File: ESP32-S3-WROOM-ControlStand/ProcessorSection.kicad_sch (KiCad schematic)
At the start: 21 parts, among them IC601 USBLC6-2SC6, J601 GCT_USB4105, SW24 RESET, SW601 BOOT, U601 ESP32_S3_WROOM-1

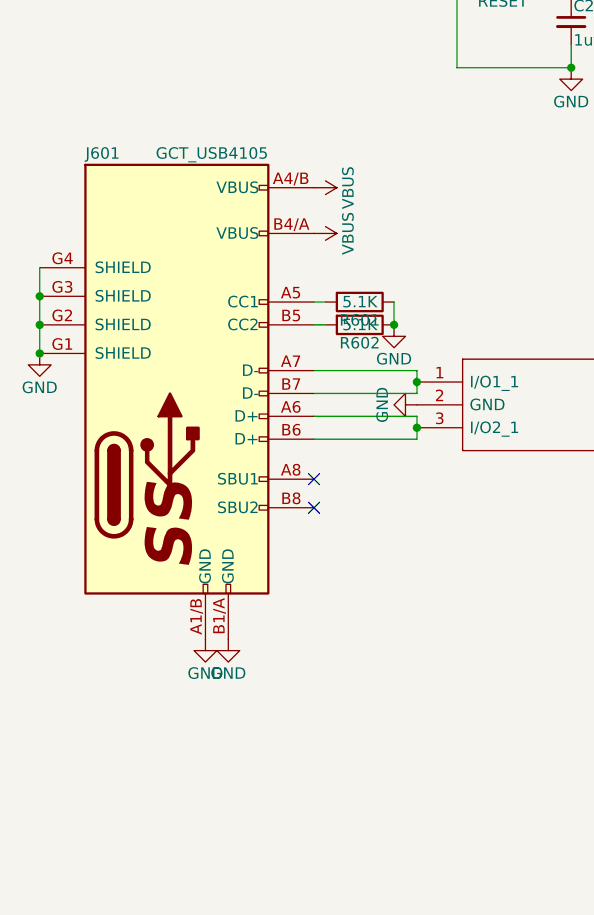
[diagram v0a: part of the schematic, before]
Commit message: 3D models mostly done.
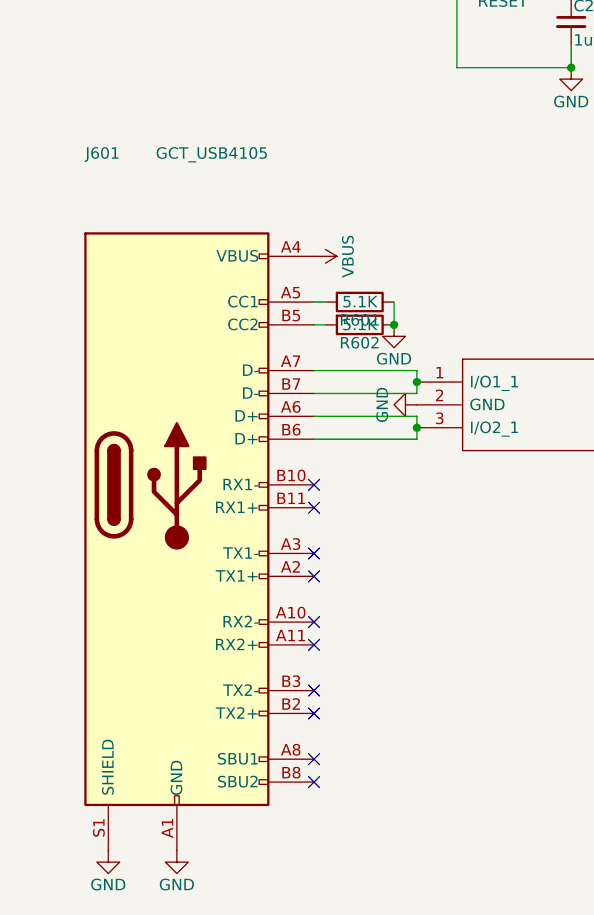
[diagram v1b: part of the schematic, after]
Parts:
- IC601: footprint TO_SOT_Packages_SMD:SOT-23-6 -> Package_TO_SOT_SMD:SOT-23-6
- J601: footprint GCT_USB:GCT_USB4105-GF-A -> Connector_USB:USB_C_Receptacle_GCT_USB4105-xx-A_16P_TopMnt_Horizontal; symbol gct_usb4105:GCT_USB4105 -> Connector:USB_C_Receptacle
- SW24: footprint Buttons_Switches_SMD:SW_SPST_PTS810 -> Button_Switch_SMD:SW_SPST_PTS810
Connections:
- net GND: now also J601.A1 (GND), J601.A12 (GND), J601.B1 (GND), J601.B12 (GND), J601.S1 (SHIELD); no longer J601.A1/B (GND), J601.B1/A (GND), J601.G1 (SHIELD), J601.G2 (SHIELD), J601.G3 (SHIELD), J601.G4 (SHIELD)
- net VBUS: now also J601.A4 (VBUS), J601.A9 (VBUS), J601.B4 (VBUS), J601.B9 (VBUS); no longer J601.A4/B (VBUS), J601.B4/A (VBUS)
- no-connect marks 12 -> 20
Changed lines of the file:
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@@
   (junction (at 73.025 139.065) (diameter 0) (color 0 0 0 0)
   )
-  (junction (at 33.655 135.89) (diameter 0) (color 0 0 0 0)
-  )
-  (junction (at 33.655 139.065) (diameter 0) (color 0 0 0 0)
-  )
   (junction (at 75.565 150.495) (diameter 0) (color 0 0 0 0)
   )
@@
   (junction (at 92.71 110.49) (diameter 0) (color 0 0 0 0)
   )
-  (junction (at 33.655 142.24) (diameter 0) (color 0 0 0 0)
-  )
   (junction (at 167.005 66.04) (diameter 0) (color 0 0 0 0)
   )
   (junction (at 92.71 101.6) (diameter 0) (color 0 0 0 0)
   )
+  (no_connect (at 64.135 174.625))
+  (no_connect (at 64.135 182.245))
   (no_connect (at 192.405 82.55))
+  (no_connect (at 64.135 187.325))
+  (no_connect (at 64.135 179.705))
   (no_connect (at 192.405 90.17))
   (no_connect (at 192.405 95.25))
   (no_connect (at 64.135 159.385))
+  (no_connect (at 64.135 167.005))
   (no_connect (at 192.405 92.71))
   (no_connect (at 192.405 102.87))
-  (no_connect (at 64.135 156.21))
+  (no_connect (at 64.135 164.465))
+  (no_connect (at 64.135 156.845))
   (no_connect (at 192.405 105.41))
+  (no_connect (at 64.135 189.865))
   (no_connect (at 141.605 87.63))
   (no_connect (at 192.405 100.33))
+  (no_connect (at 64.135 172.085))
   (no_connect (at 192.405 87.63))
   (no_connect (at 192.405 85.09))
@@
     (stroke (width 0) (type default) (color 0 0 0 0))
   )
-  (wire (pts (xy 33.655 132.715) (xy 33.655 135.89))
-    (stroke (width 0) (type default) (color 0 0 0 0))
-  )
   (wire (pts (xy 73.025 136.525) (xy 73.025 139.065))
     (stroke (width 0) (type default) (color 0 0 0 0))
   )
-  (wire (pts (xy 33.655 135.89) (xy 33.655 139.065))
-    (stroke (width 0) (type default) (color 0 0 0 0))
-  )
   (wire (pts (xy 92.71 107.95) (xy 92.71 110.49))
     (stroke (width 0) (type default) (color 0 0 0 0))
@@
   )
   (wire (pts (xy 205.74 107.95) (xy 205.74 110.49))
-    (stroke (width 0) (type default) (color 0 0 0 0))
-  )
-  (wire (pts (xy 33.655 139.065) (xy 33.655 142.24))
     (stroke (width 0) (type default) (color 0 0 0 0))
   )
@@
     )
     (property "Value" "RESET" (id 1) (at 85.09 103.124 0))
-    (property "Footprint" "Buttons_Switches_SMD:SW_SPST_PTS810" (id 2) (at 85.09 96.52 0)
+    (property "Footprint" "Button_Switch_SMD:SW_SPST_PTS810" (id 2) (at 85.09 96.52 0)
       (effects (font (size 1.27 1.27)) hide)
     )
@@
     (pin "EPad")
   )
-  (symbol (lib_id "gct_usb4105:GCT_USB4105") (at 48.895 156.845 0) (unit 1)
+  (symbol (lib_id "Connector:USB_C_Receptacle") (at 48.895 156.845 0) (unit 1)
     (in_bom yes) (on_board yes)
     (property "Reference" "J601" (id 0) (at 38.735 120.015 0)
@@
       (effects (font (size 1.27 1.27)) (justify right))
     )
-    (property "Footprint" "GCT_USB:GCT_USB4105-GF-A" (id 2) (at 52.705 156.845 0)
-      (effects (font (size 1.27 1.27)) hide)
-    )
-    (property "Datasheet" "" (id 3) (at 52.705 156.845 0)
-      (effects (font (size 1.27 1.27)) hide)
-    )
-    (pin "A1/B")
-    (pin "A4/B")
+    (property "Footprint" "Connector_USB:USB_C_Receptacle_GCT_USB4105-xx-A_16P_TopMnt_Horizontal" (id 2) (at 52.705 156.845 0)
+      (effects (font (size 1.27 1.27)) hide)
+    )
+    (property "Datasheet" "https://www.usb.org/sites/default/files/documents/usb_type-c.zip" (id 3) (at 52.705 156.845 0)
+      (effects (font (size 1.27 1.27)) hide)
+    )
+    (pin "A1")
+    (pin "A10")
+    (pin "A11")
+    (pin "A12")
+    (pin "A2")
+    (pin "A3")
+    (pin "A4")
     (pin "A5")
     (pin "A6")
     (pin "A7")
     (pin "A8")
-    (pin "B1/A")
-    (pin "B4/A")
+    (pin "A9")
+    (pin "B1")
+    (pin "B10")
+    (pin "B11")
+    (pin "B12")
+    (pin "B2")
+    (pin "B3")
+    (pin "B4")
     (pin "B5")
     (pin "B6")
     (pin "B7")
     (pin "B8")
-    (pin "G1")
-    (pin "G2")
-    (pin "G3")
-    (pin "G4")
+    (pin "B9")
+    (pin "S1")
   )
   (symbol (lib_id "USBLC6-2SC6:USBLC6-2SC6") (at 75.565 145.415 0) (unit 1)
@@
       (effects (font (size 1.27 1.27)) (justify left))
     )
-    (property "Footprint" "TO_SOT_Packages_SMD:SOT-23-6" (id 2) (at 104.775 142.875 0)
+    (property "Footprint" "Package_TO_SOT_SMD:SOT-23-6" (id 2) (at 104.775 142.875 0)
       (effects (font (size 1.27 1.27)) (justify left) hide)
     )
@@
     (pin "1")
   )
-  (symbol (lib_id "ESP32-S3-WROOM-ControlStand-rescue:VBUS") (at 64.135 123.825 270) (unit 1)
-    (in_bom yes) (on_board yes)
-    (property "Reference" "#PWR071" (id 0) (at 60.325 123.825 0)
-      (effects (font (size 1.27 1.27)) hide)
-    )
-    (property "Value" "VBUS" (id 1) (at 67.945 123.825 0))
-    (property "Footprint" "" (id 2) (at 64.135 123.825 0)
-      (effects (font (size 1.27 1.27)) hide)
-    )
-    (property "Datasheet" "" (id 3) (at 64.135 123.825 0)
-      (effects (font (size 1.27 1.27)) hide)
-    )
-    (pin "1")
-  )
-  (symbol (lib_id "ESP32-S3-WROOM-ControlStand-rescue:VBUS") (at 64.135 128.905 270) (unit 1)
-    (in_bom yes) (on_board yes)
-    (property "Reference" "#PWR072" (id 0) (at 60.325 128.905 0)
-      (effects (font (size 1.27 1.27)) hide)
-    )
-    (property "Value" "VBUS" (id 1) (at 67.945 128.905 0))
-    (property "Footprint" "" (id 2) (at 64.135 128.905 0)
-      (effects (font (size 1.27 1.27)) hide)
-    )
-    (property "Datasheet" "" (id 3) (at 64.135 128.905 0)
-      (effects (font (size 1.27 1.27)) hide)
-    )
-    (pin "1")
-  )
-  (symbol (lib_id "ESP32-S3-WROOM-ControlStand-rescue:GND") (at 54.61 173.99 0) (unit 1)
-    (in_bom yes) (on_board yes)
-    (property "Reference" "#PWR073" (id 0) (at 54.61 180.34 0)
-      (effects (font (size 1.27 1.27)) hide)
-    )
-    (property "Value" "GND" (id 1) (at 54.61 177.8 0))
-    (property "Footprint" "" (id 2) (at 54.61 173.99 0)
-      (effects (font (size 1.27 1.27)) hide)
-    )
-    (property "Datasheet" "" (id 3) (at 54.61 173.99 0)
-      (effects (font (size 1.27 1.27)) hide)
-    )
-    (pin "1")
-  )
-  (symbol (lib_id "ESP32-S3-WROOM-ControlStand-rescue:GND") (at 52.07 173.99 0) (unit 1)
-    (in_bom yes) (on_board yes)
-    (property "Reference" "#PWR074" (id 0) (at 52.07 180.34 0)
-      (effects (font (size 1.27 1.27)) hide)
-    )
-    (property "Value" "GND" (id 1) (at 52.07 177.8 0))
-    (property "Footprint" "" (id 2) (at 52.07 173.99 0)
-      (effects (font (size 1.27 1.27)) hide)
-    )
-    (property "Datasheet" "" (id 3) (at 52.07 173.99 0)
-      (effects (font (size 1.27 1.27)) hide)
-    )
-    (pin "1")
-  )
-  (symbol (lib_id "ESP32-S3-WROOM-ControlStand-rescue:GND") (at 33.655 142.24 0) (unit 1)
-    (in_bom yes) (on_board yes)
-    (property "Reference" "#PWR075" (id 0) (at 33.655 148.59 0)
-      (effects (font (size 1.27 1.27)) hide)
-    )
-    (property "Value" "GND" (id 1) (at 33.655 146.05 0))
-    (property "Footprint" "" (id 2) (at 33.655 142.24 0)
-      (effects (font (size 1.27 1.27)) hide)
-    )
-    (property "Datasheet" "" (id 3) (at 33.655 142.24 0)
-      (effects (font (size 1.27 1.27)) hide)
-    )
+  (symbol (lib_id "ESP32-S3-WROOM-ControlStand-rescue:VBUS") (at 64.135 131.445 270) (unit 1)
+    (in_bom yes) (on_board yes)
+    (property "Reference" "#PWR072" (id 0) (at 60.325 131.445 0)
+      (effects (font (size 1.27 1.27)) hide)
+    )
+    (property "Value" "VBUS" (id 1) (at 67.945 131.445 0))
+    (property "Footprint" "" (id 2) (at 64.135 131.445 0)
+      (effects (font (size 1.27 1.27)) hide)
+    )
+    (property "Datasheet" "" (id 3) (at 64.135 131.445 0)
+      (effects (font (size 1.27 1.27)) hide)
+    )
+    (pin "1")
+  )
+  (symbol (lib_id "ESP32-S3-WROOM-ControlStand-rescue:GND") (at 48.895 197.485 0) (unit 1)
+    (in_bom yes) (on_board yes)
+    (property "Reference" "#PWR073" (id 0) (at 48.895 203.835 0)
+      (effects (font (size 1.27 1.27)) hide)
+    )
+    (property "Value" "GND" (id 1) (at 48.895 201.295 0))
+    (property "Footprint" "" (id 2) (at 48.895 197.485 0)
+      (effects (font (size 1.27 1.27)) hide)
+    )
+    (property "Datasheet" "" (id 3) (at 48.895 197.485 0)
+      (effects (font (size 1.27 1.27)) hide)
+    )
+    (pin "1")
+  )
+  (symbol (lib_id "ESP32-S3-WROOM-ControlStand-rescue:GND") (at 41.275 197.485 0) (unit 1)
+    (in_bom yes) (on_board yes)
+    (property "Reference" "#PWR074" (id 0) (at 41.275 203.835 0)
+      (effects (font (size 1.27 1.27)) hide)
+    )
+    (property "Value" "GND" (id 1) (at 41.275 201.295 0))
+    (property "Footprint" "" (id 2) (at 41.275 197.485 0)
+      (effects (font (size 1.27 1.27)) hide)
+    )
+    (property "Datasheet" "" (id 3) (at 41.275 197.485 0)
+      (effects (font (size 1.27 1.27)) hide)
+    )

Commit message: Finalize part numbers for BOM.
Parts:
- J601: Mouser Part Number (none) -> 640-USB4105-GF-A-120
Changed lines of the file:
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@@
+      (effects (font (size 1.27 1.27)) hide)
+    )
+    (property "Mouser Part Number" "640-USB4105-GF-A-120" (id 4) (at 48.895 156.845 0)
       (effects (font (size 1.27 1.27)) hide)
     )
